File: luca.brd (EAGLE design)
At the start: 71 x 72 mm, 60 parts

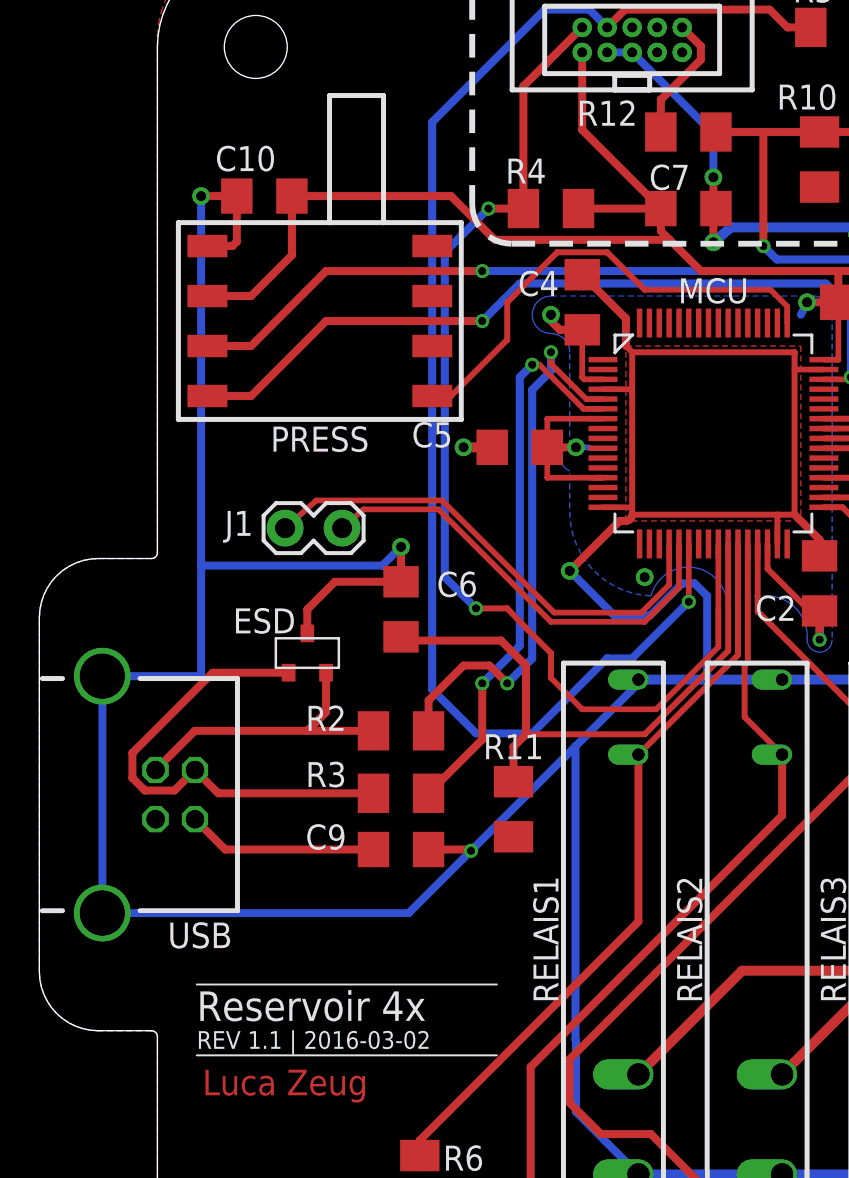
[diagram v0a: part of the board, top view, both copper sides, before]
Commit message: Refactoring ESD, NMI
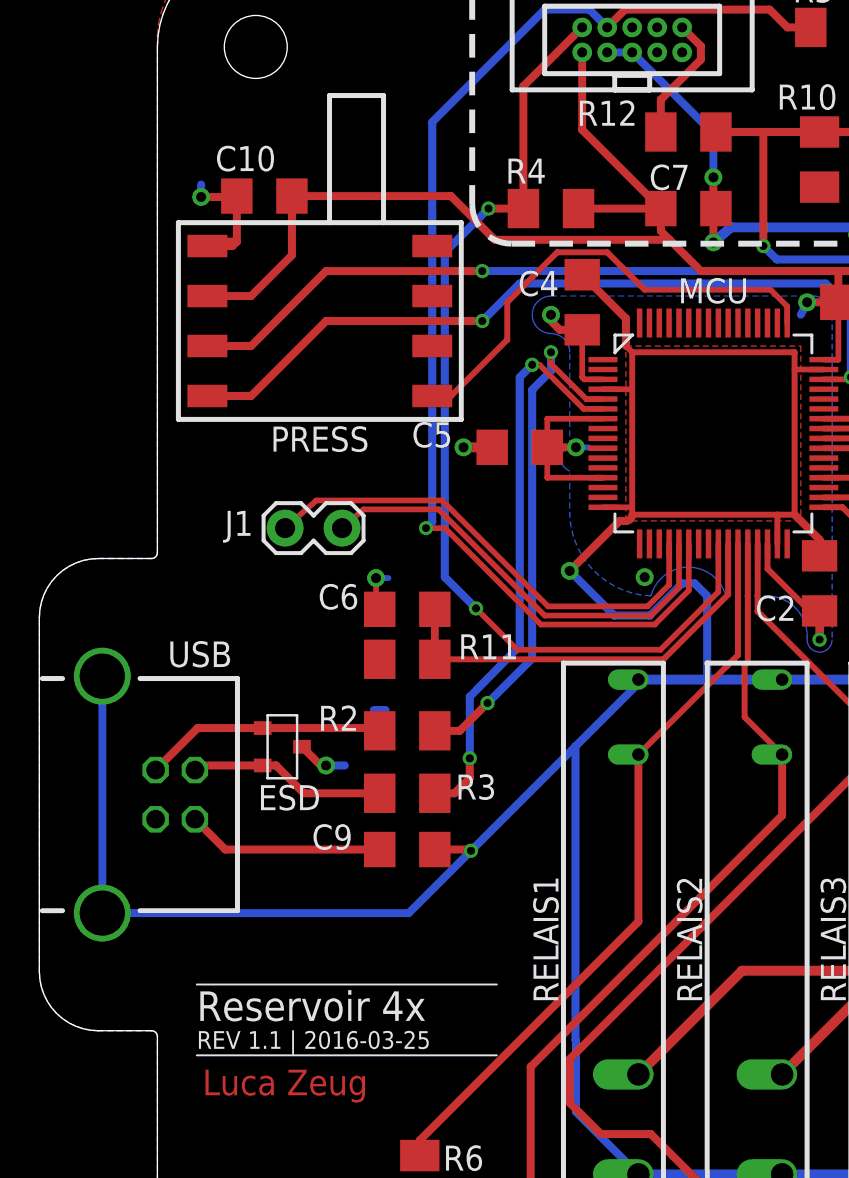
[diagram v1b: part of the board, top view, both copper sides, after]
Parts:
- moved R11 9.34 mm to (12.7, 35.9), turned to 0 degrees
- moved ESD 4.93 mm to (6.35, 31.4), turned to 90 degrees
- moved C6 0.32 mm to (12.7, 38.4), turned to 180 degrees
- moved C9 0.32 mm to (12.7, 26.2)
- moved R2 0.32 mm to (12.7, 32.2)
- moved R3 0.32 mm to (12.7, 29.1)
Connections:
- net N$1: now also ESD.P$1; no longer ESD.P$2
- net N$2: now also ESD.P$2; no longer ESD.P$1
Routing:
- net GND: track 353.2 -> 312.1 mm, vias 11 -> 12
- net N$2: track 24.3 -> 10.1 mm
- net SWD_CLK: track 71.3 -> 62.0 mm
- net NMI_B: track 30.6 -> 21.4 mm
- net SWD_DIO: track 55.9 -> 51.0 mm
- net N$1: track 15.2 -> 12.3 mm
- net USB_DP: track 28.4 -> 26.4 mm
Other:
- board text added: "REV 1.1 | 2016-03-25"
- board text removed: "REV 1.1 | 2016-03-02"

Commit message: fixed Jumper
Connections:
- removed net N$12: J1.1, MCU.20
- net VDD: now also J1.1
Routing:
- net N$12: track 24.8 -> 0.00 mm
- net VDD: track 156.8 -> 166.9 mm
- net GND: track 312.1 -> 312.8 mm
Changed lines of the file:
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@@
 <via x="11.1125" y="40.005" extent="1-16" drill="0.508"/>
 <wire x1="11.1125" y1="40.005" x2="11.7475" y2="40.005" width="0.29" layer="16"/>
-<wire x1="3.9" y1="59.4" x2="4.0375" y2="59.42" width="0" layer="19" extent="1-1"/>
+<wire x1="3.9" y1="59.4" x2="3.81" y2="59.49" width="0.29" layer="1"/>
+<wire x1="3.81" y1="59.49" x2="3.81" y2="60.0125" width="0.29" layer="1"/>
 </signal>
 <signal name="N$1">
@@
 <wire x1="22.6441" y1="45.104990625" x2="19.815" y2="45.104990625" width="0.29" layer="1"/>
 <wire x1="19.815" y1="45.104990625" x2="19.815" y2="46.65" width="0.29" layer="1"/>
+<contactref element="J1" pad="1"/>
+<wire x1="6.4897" y1="42.545" x2="6.4897" y2="38.2778" width="0.29" layer="1"/>
+<wire x1="6.4897" y1="38.2778" x2="8.89" y2="35.8775" width="0.29" layer="1"/>
+<wire x1="8.89" y1="35.8775" x2="11.3" y2="35.8775" width="0.29" layer="1"/>
 </signal>
 <signal name="VCC">
@@
 <contactref element="MCU" pad="15"/>
 </signal>
-<signal name="N$12">
-<contactref element="MCU" pad="20"/>
-<contactref element="J1" pad="1"/>
-<wire x1="26.007490625" y1="41.7416" x2="26.007490625" y2="39.659990625" width="0.29" layer="1"/>
-<wire x1="24.915" y1="38.5675" x2="19.8525" y2="38.5675" width="0.29" layer="1"/>
-<wire x1="14.47" y1="43.95" x2="8.0772" y2="43.95" width="0.29" layer="1"/>
-<wire x1="8.0772" y1="43.95" x2="6.4897" y2="42.545" width="0.29" layer="1"/>
-<wire x1="26.007490625" y1="39.659990625" x2="24.915" y2="38.5675" width="0.29" layer="1"/>
-<wire x1="14.47" y1="43.95" x2="19.8525" y2="38.5675" width="0.29" layer="1"/>
-</signal>
 <signal name="N$13">
